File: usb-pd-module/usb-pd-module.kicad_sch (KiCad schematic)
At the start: 28 parts, among them J1 USBC, J2 OUT, Q1 AO3407A, U1 CH221K, U2 SPX1117M3

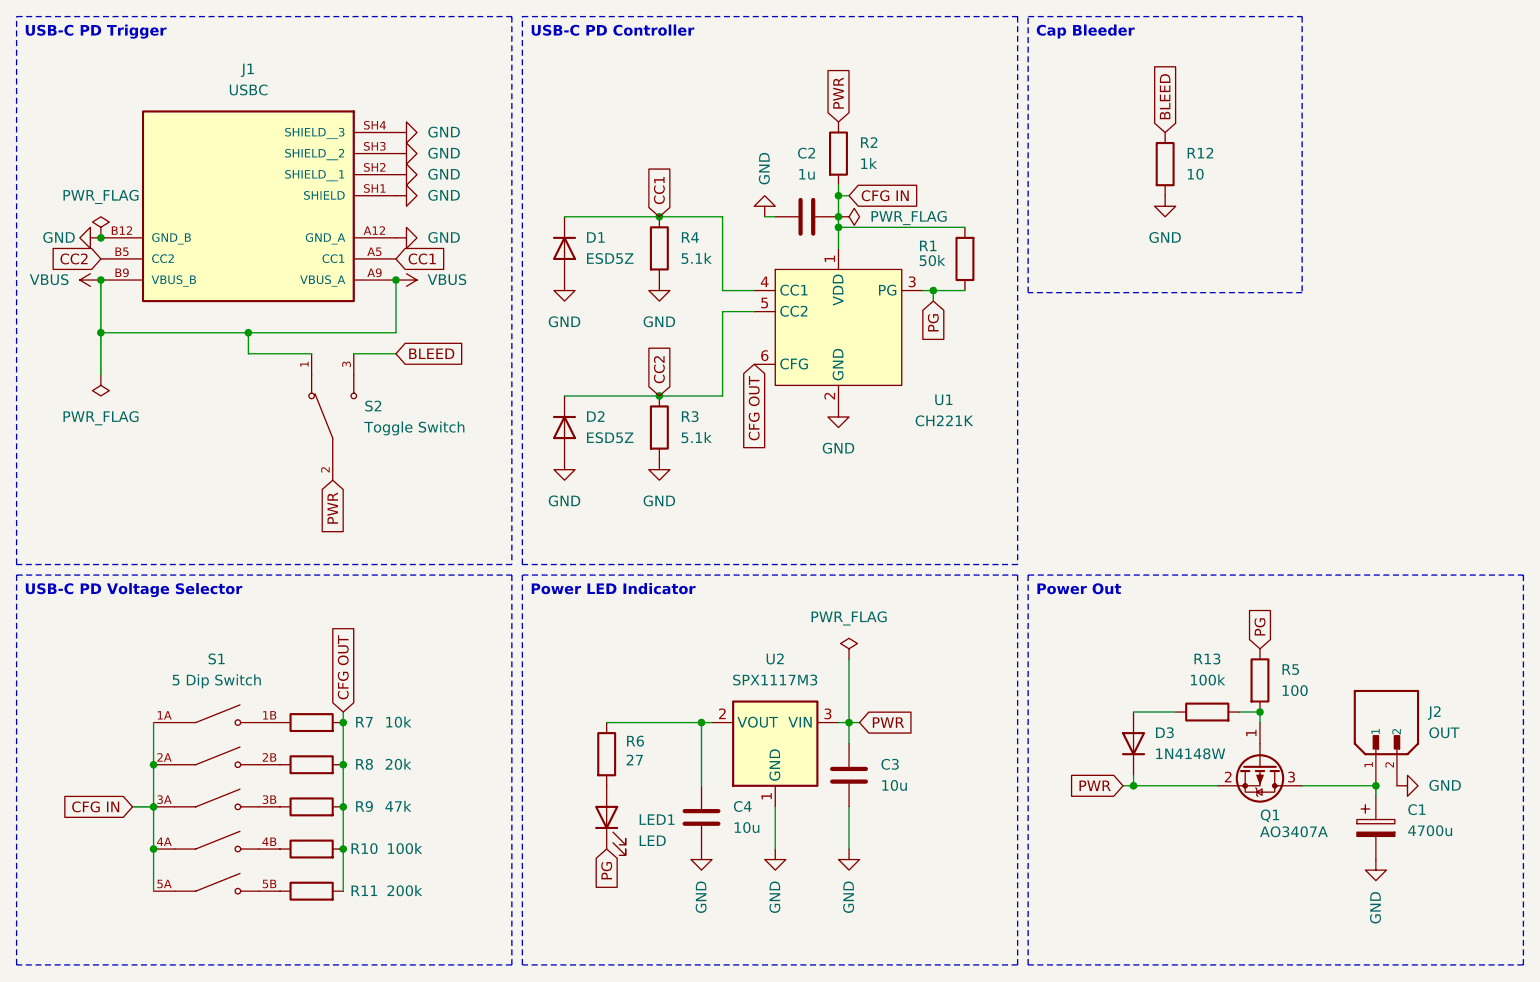
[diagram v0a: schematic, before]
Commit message: Update USB PD Module to Rev 4.5 with improved power path and RGB LED indicator
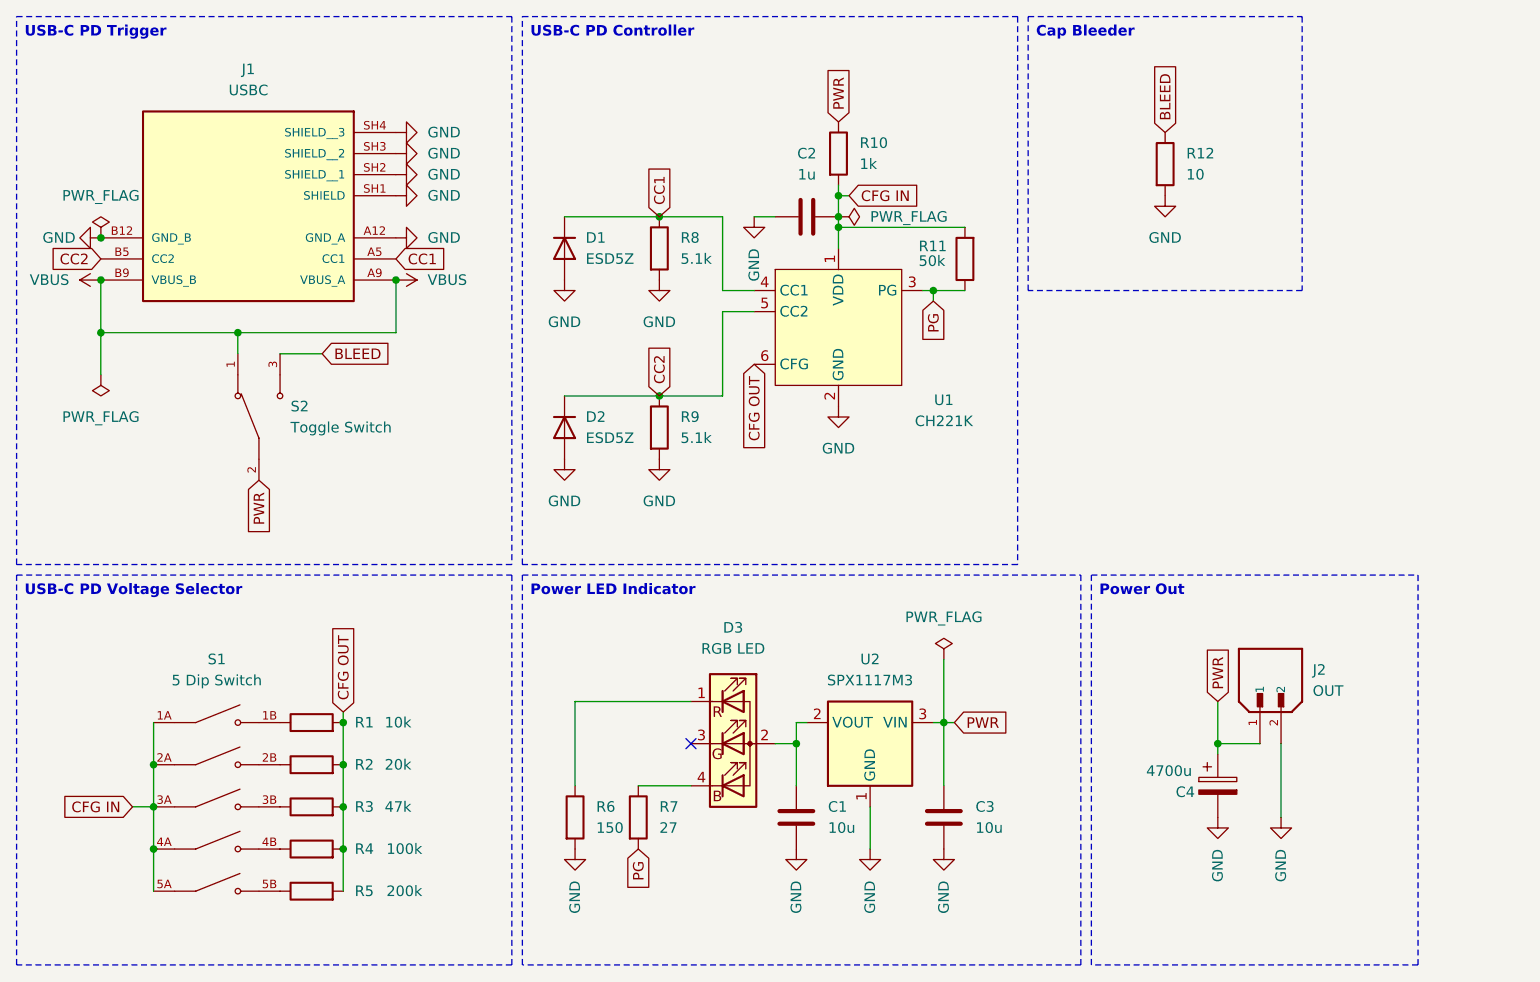
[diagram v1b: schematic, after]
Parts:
- removed D3: 1N4148W, Diode_SMD:D_SOD-123, symbol Diode:1N4148W
- removed LED1: LED, LED_THT:LED_D5.0mm, symbol Device:LED
- removed Q1: AO3407A, Package_TO_SOT_SMD:SOT-23, symbol Transistor_FET:AO3401A
- removed R13: 100k, Resistor_SMD:R_0603_1608Metric_Pad0.98x0.95mm_HandSolder, symbol Device:R
- removed R5: 100, Resistor_SMD:R_0603_1608Metric_Pad0.98x0.95mm_HandSolder, symbol Device:R
- added D3: RGB LED, LED_THT:LED_D5.0mm-4_RGB, symbol Device:LED_RAGB
- added R7: 27, Resistor_SMD:R_0603_1608Metric_Pad0.98x0.95mm_HandSolder, symbol Device:R
- R6: value 27 -> 150
- renumbered C4 to C1, C1 to C4, R7 to R1, R2 to R10, R1 to R11, R8 to R2, R9 to R3, R10 to R4, R11 to R5, R4 to R8, R3 to R9
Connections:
- net GND: now also R6.2
- net PG: now also R7.2
- net PWR: now also C4.1, J2.1
- net at C1.2, U2.2 (VOUT): now also D3.2 (A); no longer R6.1
- new net: D3.1 (RK), R6.1
- new net: D3.4 (BK), R7.1
- no-connect marks 0 -> 1
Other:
- moved on the sheet: C1, C3, C4, J2, S2, U2

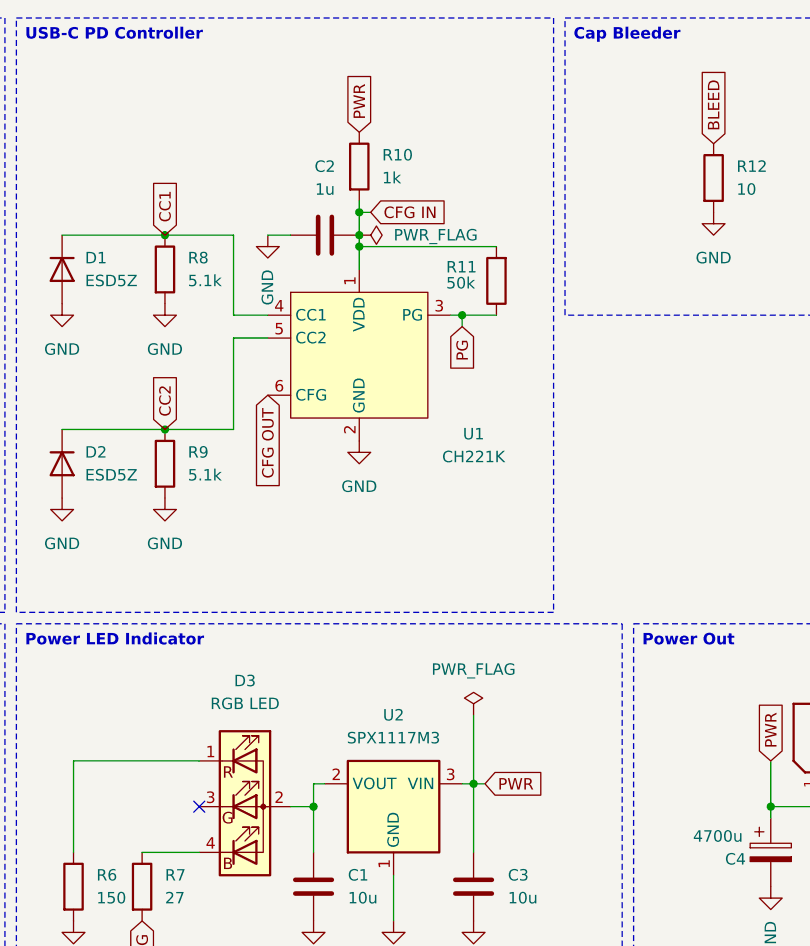
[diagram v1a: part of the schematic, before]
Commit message: Update CH221K Pin Good path to LDO 3.3volts
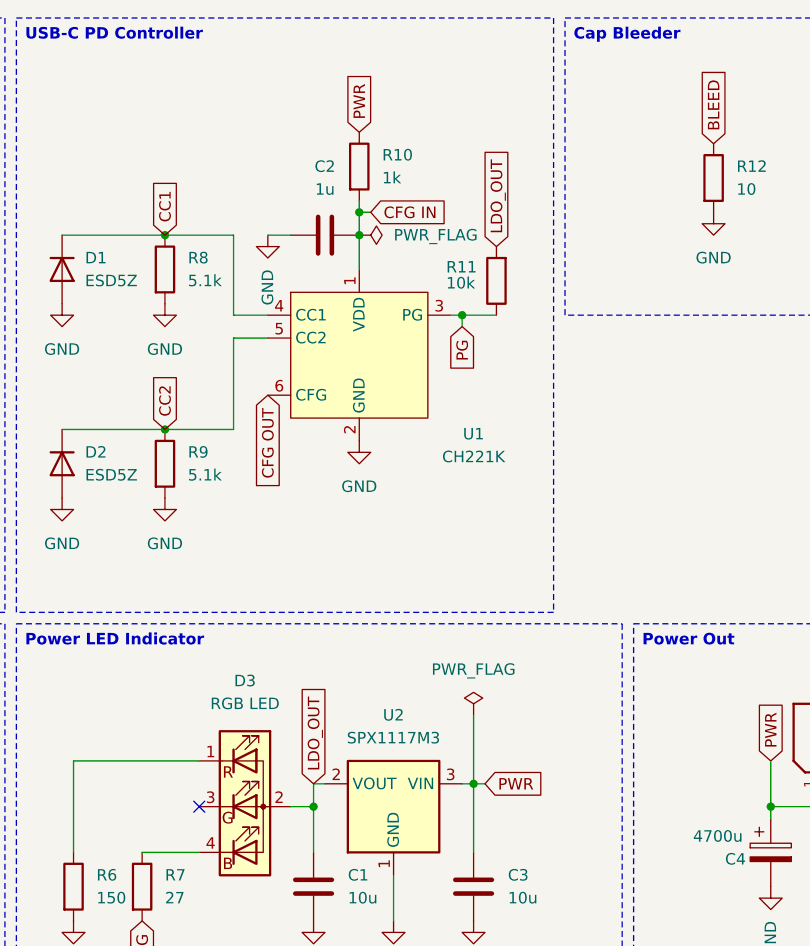
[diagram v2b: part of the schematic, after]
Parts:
- R11: value 50k -> 10k
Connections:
- net CFG IN: no longer R11.2
- net LDO_OUT: now reaches C1.2, D3.2 (A), U2.2 (VOUT)
- net LDO_OUT: now also R11.2
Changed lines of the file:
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@@
-	)
-	(junction
-		(at 116.84 43.18)
-		(diameter 0)
-		(color 0 0 0 0)
 	)
 	(junction
@@
 	(wire
 		(pts
-			(xy 116.84 43.18) (xy 116.84 45.72)
-		)
-		(stroke
-			(width 0)
-			(type default)
-		)
-	)
-	(wire
-		(pts
-			(xy 132.08 43.18) (xy 116.84 43.18)
+			(xy 116.84 41.91) (xy 116.84 45.72)
 		)
 		(stroke
@@
 	(wire
 		(pts
-			(xy 116.84 41.91) (xy 116.84 43.18)
-		)
-		(stroke
-			(width 0)
-			(type default)
-		)
-	)
-	(wire
-		(pts
 			(xy 111.76 105.41) (xy 111.76 110.49)
 		)
@@
 		(property "Intersheetrefs" "${INTERSHEET_REFS}"
 			(at 116.84 23.5034 90)
+			(effects
+				(font
+					(size 1.27 1.27)
+				)
+				(justify left)
+				(hide yes)
+			)
+		)
+	)
+	(global_label "LDO_OUT"
+		(shape input)
+		(at 111.76 102.87 90)
+		(fields_autoplaced yes)
+		(effects
+			(font
+				(size 1.27 1.27)
+			)
+			(justify left)
+		)
+		(property "Intersheetrefs" "${INTERSHEET_REFS}"
+			(at 111.76 91.66 90)
+			(effects
+				(font
+					(size 1.27 1.27)
+				)
+				(justify left)
+				(hide yes)
+			)
+		)
+	)
+	(global_label "LDO_OUT"
+		(shape input)
+		(at 132.08 43.18 90)
+		(fields_autoplaced yes)
+		(effects
+			(font
+				(size 1.27 1.27)
+			)
+			(justify left)
+		)
+		(property "Intersheetrefs" "${INTERSHEET_REFS}"
+			(at 132.08 31.97 90)
 			(effects
 				(font
@@
 			)
 		)
-		(property "Value" "50k"
+		(property "Value" "10k"
 			(at 126.492 47.244 0)
 			(effects
